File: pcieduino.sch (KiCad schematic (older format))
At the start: 8 parts, among them IC1 ATMEGA328P-A, SW1 SW_PUSH, X1 CRYSTAL

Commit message: add recent more progress
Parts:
- added C5, C6: C, ~, symbol C
- added D1: RED_RX, ~, symbol LED
- added D2: GREEN_TX, ~, symbol LED
- added J1: PCIE-MINI, MODULE, symbol PCIE-MINI
- added R2, R3: 390, ~, symbol R
- added U1: FT232RL, symbol FT232RL
- X1: value CRYSTAL -> 8MHz
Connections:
- net labels added: USB_M, USB_P
- wire segments 21 -> 49
- no-connect marks 3 -> 63
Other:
- moved on the sheet: C1, C2, C3, C4, IC1, R1, SW1, X1

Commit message: finished first draft of schematic
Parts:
- removed C6: C, ~, symbol C
- added C6: 10u, ~, symbol CP1
- added C7, C8: 0.1u, ~, symbol C
- added D3: LED, ~, symbol LED
- added F1: FUSE, ~, symbol FUSE
- added J2: DIGITAL2, ~, symbol CONN_8
- added J3: POWER, ~, symbol CONN_6
- added J4: ISP, ~, symbol CONN_3X2
- added J5: ANALOG, ~, symbol CONN_6
- added J6: DIGITAL, ~, symbol CONN_8
- added R4: R, ~, symbol R
- added R5, R6: 1K, ~, symbol R
- C1, C4: value C -> 0.1u
- C2, C3: value C -> 22p
- R1: value R -> 10K
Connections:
- wire segments 49 -> 81
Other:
- moved on the sheet: C2, C3, D1, D2, J1, R2, R3, X1

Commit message: update connections
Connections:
- net labels added: D11/MOSI, D12/MISO, D13/SCK
- net labels removed: MISO, MOSI, SCK
- wire segments 81 -> 96
- no-connect marks 63 -> 50
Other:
- moved on the sheet: C1, C2, C3, C4, C5, D1, D2, F1, IC1, J5, J6, R1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

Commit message: latest updates starting to work on the PCB
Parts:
- C1: footprint ~ -> SM0603_Capa; Seed PN (none) -> 0100020P1
- C5: value C -> 0.1u; footprint ~ -> SM0603_Capa; Seed PN (none) -> 0100020P1
- R1, R2, R3, R5, R6: footprint ~ -> SM0603_Resistor
- R4: value R -> 390; footprint ~ -> SM0603_Resistor
- U1: footprint (none) -> SSOP28
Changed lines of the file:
@@
 Sheet 1 1
 Title "PCIeDuino328v1"
-Date "28 aug 2014"
+Date "10 oct 2014"
 Rev "1"
 Comp "moonpunch.org"
@@
 F 0 "R1" V 10380 2500 40  0000 C CNN
 F 1 "10K" V 10307 2501 40  0000 C CNN
-F 2 "~" V 10230 2500 30  0000 C CNN
+F 2 "SM0603_Resistor" V 10230 2500 30  0000 C CNN
 F 3 "~" H 10300 2500 30  0000 C CNN
 	1    10300 2500
@@
 F 0 "C1" H 6550 2250 40  0000 L CNN
 F 1 "0.1u" H 6556 2065 40  0000 L CNN
-F 2 "~" H 6588 2000 30  0000 C CNN
+F 2 "SM0603_Capa" H 6588 2000 30  0000 C CNN
 F 3 "~" H 6550 2150 60  0000 C CNN
+F 4 "0100020P1" H 6550 2150 60  0001 C CNN "Seed PN"
 	1    6550 2150
 	1    0    0    -1
@@
 F 0 "U1" H 3000 3100 60  0000 C CNN
 F 1 "FT232RL" H 3500 2100 60  0000 C CNN
-F 2 "" H 4100 2100 60  0000 C CNN
+F 2 "SSOP28" H 4150 1100 60  0000 C CNN
 F 3 "" H 4100 2100 60  0000 C CNN
 	1    3500 2100
@@
 F 0 "R2" V 4980 1850 40  0000 C CNN
 F 1 "390" V 4907 1851 40  0000 C CNN
-F 2 "~" V 4830 1850 30  0000 C CNN
+F 2 "SM0603_Resistor" V 4830 1850 30  0000 C CNN
 F 3 "~" H 4900 1850 30  0000 C CNN
 	1    4900 1850
@@
 F 0 "R3" V 5330 1850 40  0000 C CNN
 F 1 "390" V 5257 1851 40  0000 C CNN
-F 2 "~" V 5180 1850 30  0000 C CNN
+F 2 "SM0603_Resistor" V 5180 1850 30  0000 C CNN
 F 3 "~" H 5250 1850 30  0000 C CNN
 	1    5250 1850
@@
 P 2200 2950
 F 0 "C5" H 2200 3050 40  0000 L CNN
-F 1 "C" H 2206 2865 40  0000 L CNN
-F 2 "~" H 2238 2800 30  0000 C CNN
+F 1 "0.1u" H 2206 2865 40  0000 L CNN
+F 2 "SM0603_Capa" H 2238 2800 30  0000 C CNN
 F 3 "~" H 2200 2950 60  0000 C CNN
+F 4 "0100020P1" H 2200 2950 60  0001 C CNN "Seed PN"
 	1    2200 2950
 	1    0    0    -1
@@
 F 0 "R5" V 9300 3200 40  0000 C CNN
 F 1 "1K" V 9257 2951 40  0000 C CNN
-F 2 "~" V 9180 2950 30  0000 C CNN
+F 2 "SM0603_Resistor" V 9180 2950 30  0000 C CNN
 F 3 "~" H 9250 2950 30  0000 C CNN
 	1    9250 2950
@@
 F 0 "R6" V 9200 3300 40  0000 C CNN
 F 1 "1K" V 9257 3051 40  0000 C CNN
-F 2 "~" V 9180 3050 30  0000 C CNN
+F 2 "SM0603_Resistor" V 9180 3050 30  0000 C CNN
 F 3 "~" H 9250 3050 30  0000 C CNN
 	1    9250 3050
@@
 P 5600 5300
 F 0 "R4" V 5680 5300 40  0000 C CNN
-F 1 "R" V 5607 5301 40  0000 C CNN
-F 2 "~" V 5530 5300 30  0000 C CNN
+F 1 "390" V 5607 5301 40  0000 C CNN
+F 2 "SM0603_Resistor" V 5530 5300 30  0000 C CNN
 F 3 "~" H 5600 5300 30  0000 C CNN
 	1    5600 5300
@@
 Connection ~ 3600 7200
 Connection ~ 3400 7200
-Connection ~ 6100 3300
 Text Label 7300 5050 2    60   ~ 0
 AREF

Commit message: work in progress
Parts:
- removed C5: 0.1u, SM0603_Capa, symbol C
- removed U1: FT232RL, SSOP28, symbol FT232RL
- added C1, C2: 10p, ~, symbol C
- added R1: 550, ~, symbol R
- added U1: MCP2200, symbol MCP2200
- added X1: 12MHz, ~, symbol CRYSTAL
- C4: renamed from C2; value 22p -> 10p
- C5: renamed from C3; value 22p -> 10p
- D1: value RED_RX -> LED; P/N (none) -> LS L29K-G1H2-1-Z
- D2: value GREEN_TX -> LED
- D3: P/N (none) -> LB Q39G-L2N2-35-1
- R2: value 390 -> R; footprint SM0603_Resistor -> ~
- R3: value 390 -> 550; footprint SM0603_Resistor -> ~
- R4: value 390 -> 100
- X2: renamed from X1; P/N (none) -> ABM3B-8.000MHZ-10-1UT
- renumbered C1 to C3, C4 to C8, C8 to C9, R1 to R7
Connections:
- wire segments 96 -> 101
- no-connect marks 50 -> 46
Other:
- note added: "MCP2200 Section is based on\nhttp://blog.stevemarple.co.uk/2013/01/uart-usb-converter-for-mixed-33v5v.html"

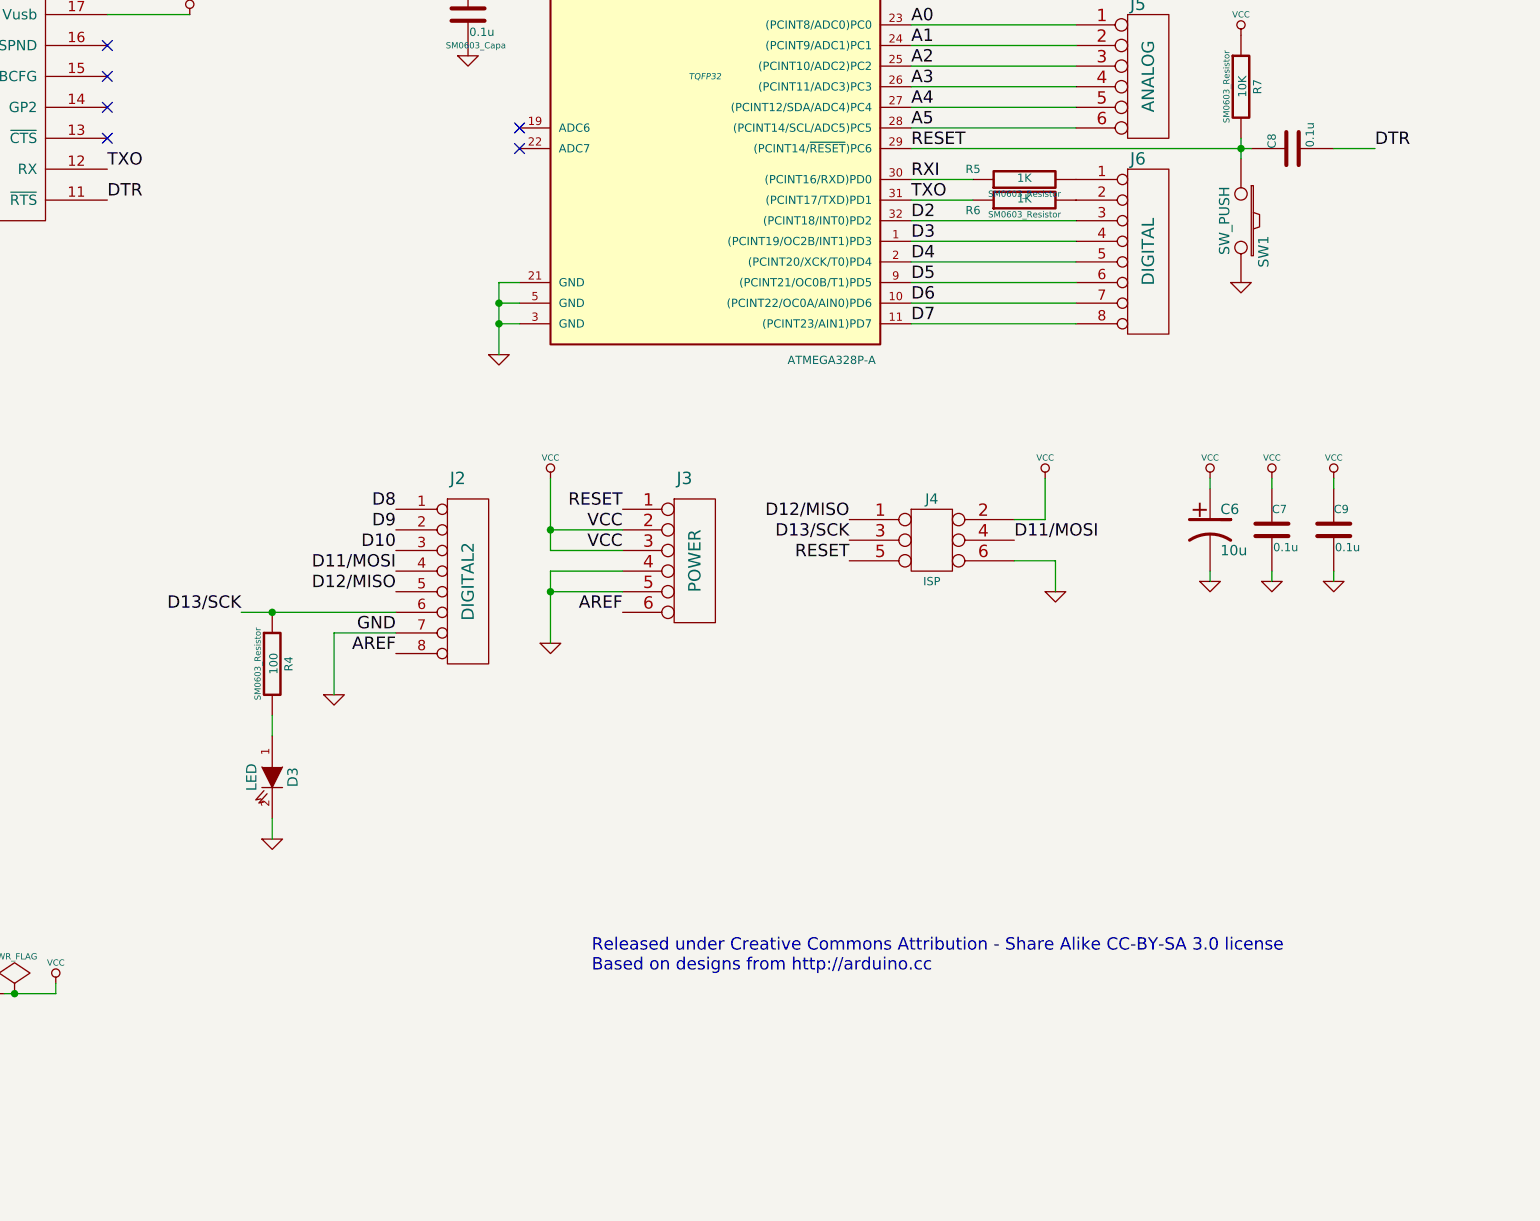
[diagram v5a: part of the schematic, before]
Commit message: add progress on 01/03
Quick summary:

* new crystal footprint
* new switch footprint
* combining digital pins
* adding mounting holes

... and some small positioning changes
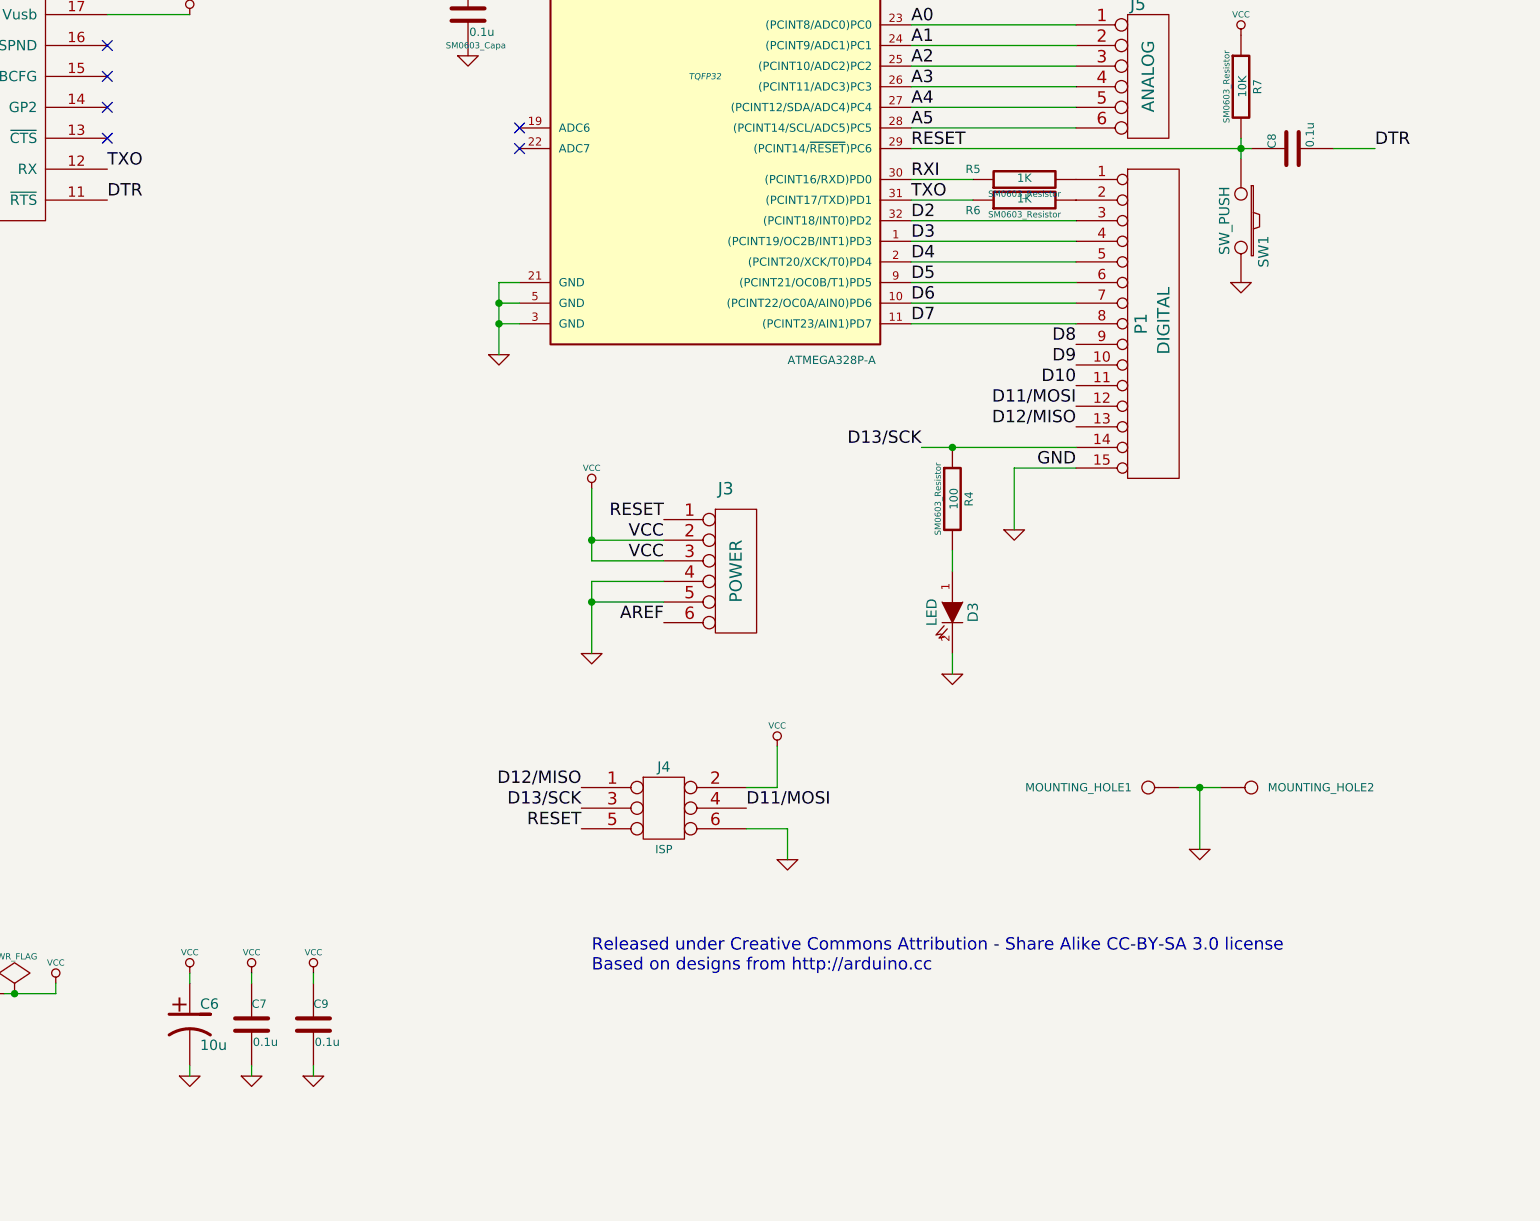
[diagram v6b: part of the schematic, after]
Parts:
- removed J2: DIGITAL2, ~, symbol CONN_8
- removed J6: DIGITAL, ~, symbol CONN_8
- added MOUNTING_HOLE1, MOUNTING_HOLE2: CONN_1, ~, symbol CONN_1
- added P1: DIGITAL, ~, symbol CONN_15
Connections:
- net D10: now also P1.11 (P11)
- net D11/MOSI: now also P1.12 (P12)
- net D12/MISO: now also P1.13 (P13)
- net D13/SCK: now also P1.14 (P14)
- net D2: now also P1.3 (P3)
- net D3: now also P1.4 (P4)
- net D4: now also P1.5 (P5)
- net D5: now also P1.6 (P6)
- net D6: now also P1.7 (P7)
- net D7: now also P1.8 (P8)
- net D8: now also P1.9 (P9)
- net D9: now also P1.10 (P10)
- net GND: now also MOUNTING_HOLE1.1, MOUNTING_HOLE2.1, P1.15 (P15)
- net at R5.2: now also P1.1 (P1)
- net at R6.2: now also P1.2 (P2)
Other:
- moved on the sheet: C6, C7, C9, D3, J3, J4, R4

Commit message: more progress on 01/03
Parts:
- removed J5: ANALOG, ~, symbol CONN_6
- added J2: ANALOG, ~, symbol CONN_8
- renumbered J4 to J3, J3 to J4, P1 to J5
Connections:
- net A0: now also J2.1 (P1)
- net A1: now also J2.2 (P2)
- net A2: now also J2.3 (P3)
- net A3: now also J2.4 (P4)
- net A4: now also J2.5 (P5)
- net A5: now also J2.6 (P6)
- net A6: now reaches IC1.19 (ADC6)
- net A6: now also J2.7 (P7)
- net A7: now reaches IC1.22 (ADC7)
- net A7: now also J2.8 (P8)
- no-connect marks 46 -> 44
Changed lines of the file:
@@
 	1    0    0    -1
 $EndComp
-NoConn ~ 6800 2700
-NoConn ~ 6800 2800
 NoConn ~ -1100 7900
 Text Label 3200 6200 0    60   ~ 0
@@
 $EndComp
 $Comp
-L CONN_3X2 J4
+L CONN_3X2 J3
 U 1 1 53F9FD80
 P 7500 6050
-F 0 "J4" H 7500 6300 50  0000 C CNN
-F 1 "ISP" H 7500 5900 40  0000 C CNN
+F 0 "J3" H 7500 6300 50  0000 C CNN
+F 1 "ISP" V 7500 6100 60  0000 C CNN
 F 2 "~" H 7500 6050 60  0000 C CNN
 F 3 "~" H 7500 6050 60  0000 C CNN
@@
 F 3 "~" H 5200 7050 60  0000 C CNN
 	1    5200 7050
-	1    0    0    -1
-$EndComp
-$Comp
-L CONN_6 J5
-U 1 1 53FA0301
-P 9850 2450
-F 0 "J5" H 9800 2800 60  0000 C CNN
-F 1 "ANALOG" V 9850 2450 60  0000 C CNN
-F 2 "~" H 9850 2450 60  0000 C CNN
-F 3 "~" H 9850 2450 60  0000 C CNN
-	1    9850 2450
 	1    0    0    -1
 $EndComp
@@
 $EndComp
 $Comp
-L CONN_6 J3
+L CONN_6 J4
 U 1 1 53FA0B3F
 P 7850 4850
-F 0 "J3" H 7800 5250 60  0000 C CNN
+F 0 "J4" H 7800 5200 60  0000 C CNN
 F 1 "POWER" V 7850 4850 60  0000 C CNN
 F 2 "~" H 7850 4850 60  0000 C CNN
@@
 Wire Wire Line
 	9600 1950 9600 1350
-Wire Wire Line
-	8700 2700 9500 2700
-Wire Wire Line
-	8700 2600 9500 2600
-Wire Wire Line
-	8700 2500 9500 2500
-Wire Wire Line
-	8700 2400 9500 2400
-Wire Wire Line
-	8700 2300 9500 2300
-Wire Wire Line
-	8700 2200 9500 2200
 Wire Wire Line
 	7150 4450 7150 4800
@@
 Connection ~ 10100 5900
 $Comp
-L CONN_15 P1
+L CONN_15 J5
 U 1 1 54A7E504
 P 9850 3650
-F 0 "P1" V 9815 3650 60  0000 C CNN
-F 1 "DIGITAL" V 9925 3665 60  0000 C CNN
+F 0 "J5" H 9800 2800 60  0000 C CNN
+F 1 "DIGITAL" V 9900 3650 60  0000 C CNN
 F 2 "~" H 9850 3700 60  0000 C CNN
 F 3 "~" H 9850 3700 60  0000 C CNN
@@
 	1    0    0    -1
 $EndComp
+Text Label 6800 2700 2    60   ~ 0
+A6
+Text Label 6800 2800 2    60   ~ 0
+A7
+$Comp
+L CONN_8 J2
+U 1 1 54A7F47E
+P 9900 5250
+F 0 "J2" H 9850 5700 60  0000 C CNN
+F 1 "ANALOG" V 9900 5250 60  0000 C CNN
+F 2 "~" H 9900 5250 60  0000 C CNN
+F 3 "~" H 9900 5250 60  0000 C CNN
+	1    9900 5250
+	1    0    0    -1
+$EndComp
+Text Label 9550 4900 2    60   ~ 0
+A0
+Text Label 9550 5000 2    60   ~ 0
+A1
+Text Label 9550 5100 2    60   ~ 0
+A2
+Text Label 9550 5200 2    60   ~ 0
+A3
+Text Label 9550 5300 2    60   ~ 0
+A4
+Text Label 9550 5400 2    60   ~ 0
+A5
+Text Label 9550 5500 2    60   ~ 0
+A6
+Text Label 9550 5600 2    60   ~ 0
+A7
 $EndSCHEMATC
